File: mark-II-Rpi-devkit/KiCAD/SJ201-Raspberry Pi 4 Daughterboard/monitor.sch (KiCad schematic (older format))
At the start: 6 parts, among them J7 FanConnector, Q1 MMBT3904

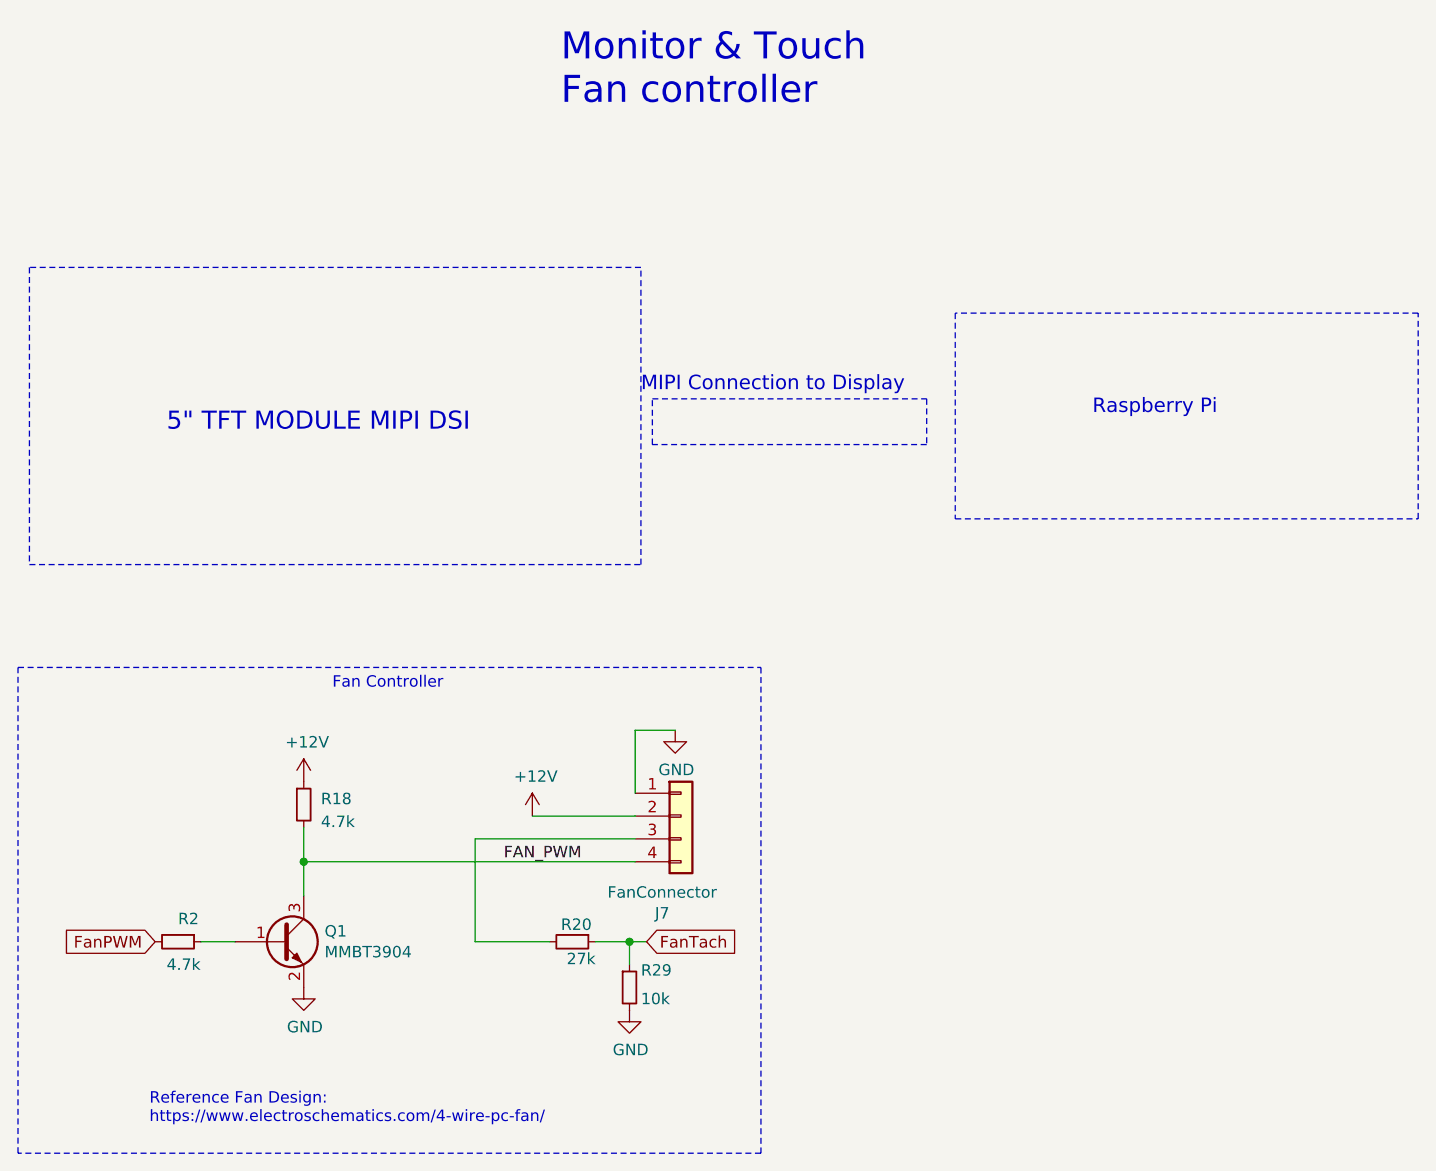
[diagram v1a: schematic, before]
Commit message: SJ-201-R6 for FAB - removed buffer IC
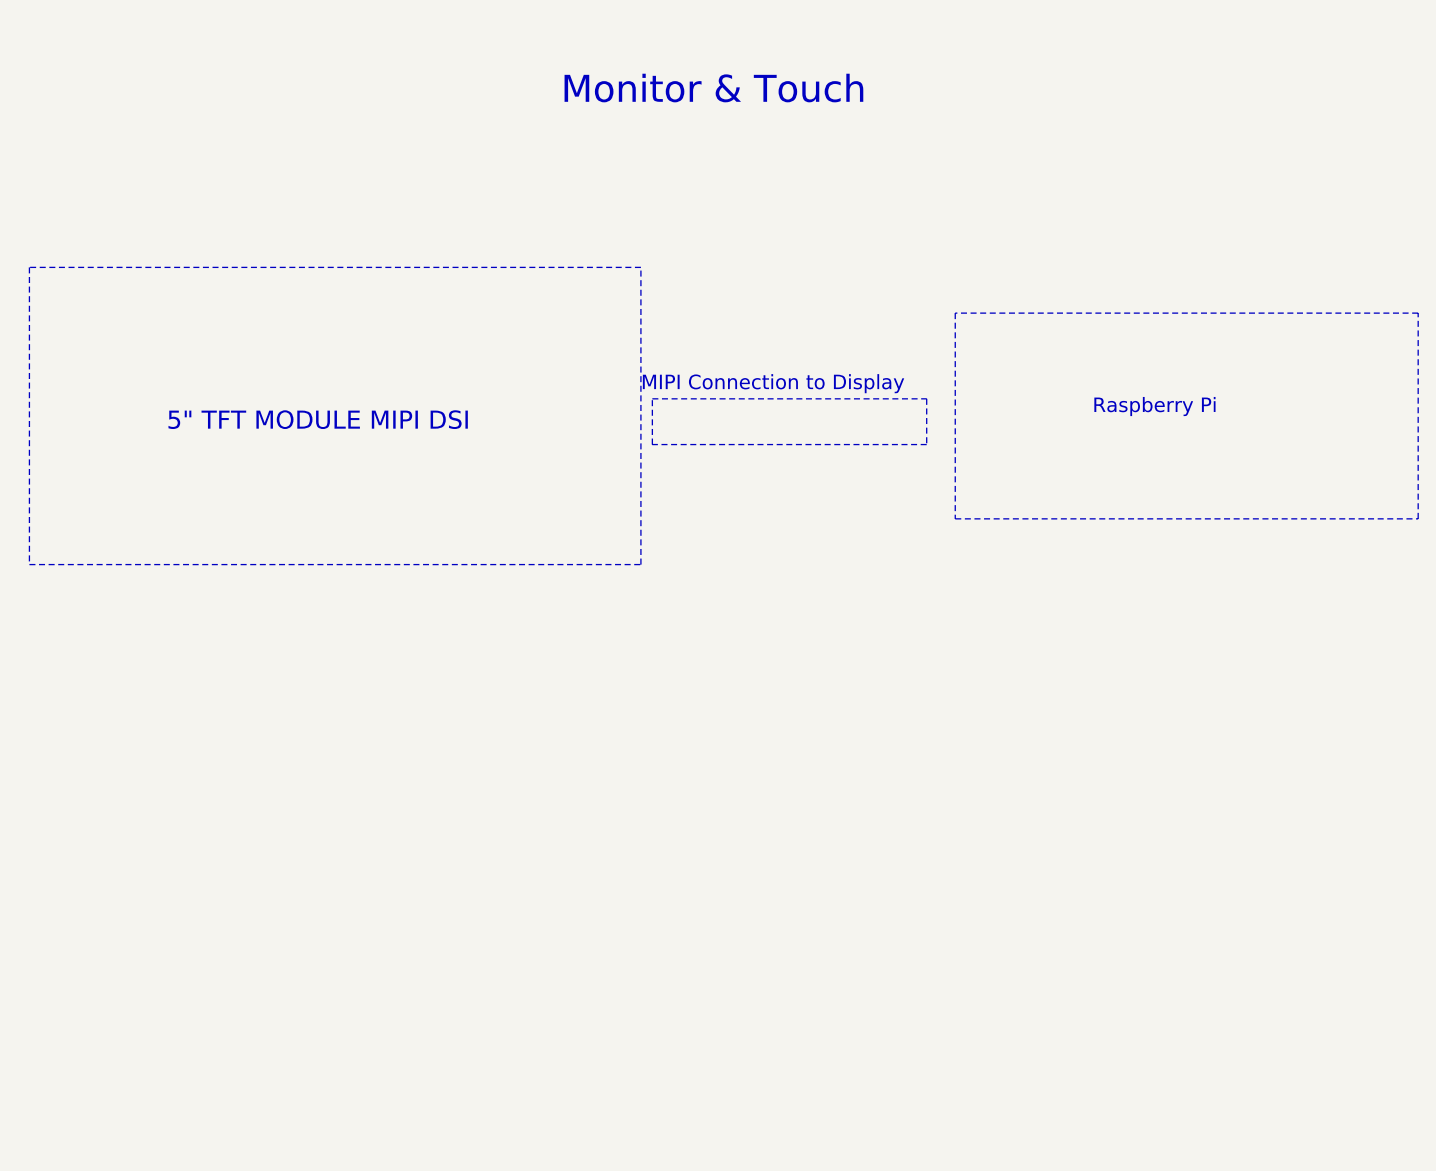
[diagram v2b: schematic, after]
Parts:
- removed J7: FanConnector, Connector:FanPinHeader_1x04_P2.54mm_Vertical, symbol Connector_Generic:Conn_01x04
- removed Q1: MMBT3904, Package_TO_SOT_SMD:SOT-23, symbol Transistor_BJT:MMBT3904
- removed R18, R2: 4.7k, Resistor_SMD:R_0402_1005Metric, symbol Device:R_Small
- removed R20: 27k, Resistor_SMD:R_0402_1005Metric, symbol Device:R_Small
- removed R29: 10k, Resistor_SMD:R_0402_1005Metric, symbol Device:R_Small
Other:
- note added: "Monitor & Touch"
- note removed: "Fan Controller"
- note removed: "Monitor & Touch\nFan controller"
- note removed: "Reference Fan Design:\nhttps://www.electroschematics.com/4-wire-pc-fan/"
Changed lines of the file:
@@
 $Descr A 11000 8500
 encoding utf-8
-Sheet 4 7
-Title ""
-Date "2020-11-22"
-Rev "Rev4 - 0.03"
-Comp "Mycroft"
-Comment1 "SJ-201-R4"
+Sheet 4 8
+Title "Monitor & Touchscreen"
+Date "2020-12-30"
+Rev "Rev5 - v1"
+Comp "Mycroft AI"
+Comment1 "SJ-201-R6"
 Comment2 ""
 Comment3 ""
@@
 $EndDescr
 Text Notes 4725 875  0    118  ~ 0
-Monitor & Touch\nFan controller
+Monitor & Touch
 Text Notes 7050 2225 0    63   ~ 0
 Raspberry Pi
@@
 Wire Notes Line
 	2400 1575 2400 2875
-$Comp
-L Transistor_BJT:MMBT3904 Q1
-U 1 1 60970DB4
-P 3500 4525
-F 0 "Q1" H 3691 4571 50  0000 L CNN
-F 1 "MMBT3904" H 3691 4480 50  0000 L CNN
-F 2 "Package_TO_SOT_SMD:SOT-23" H 3700 4450 50  0001 L CIN
-F 3 "" H 3500 4525 50  0001 L CNN
-F 4 "C20526" H 3500 4525 50  0001 C CNN "LCSC"
-	1    3500 4525
-	1    0    0    -1
-$EndComp
-$Comp
-L power:GND #PWR0117
-U 1 1 60971565
-P 3600 4725
-F 0 "#PWR0117" H 3600 4475 50  0001 C CNN
-F 1 "GND" H 3605 4552 50  0000 C CNN
-F 2 "" H 3600 4725 50  0001 C CNN
-F 3 "" H 3600 4725 50  0001 C CNN
-	1    3600 4725
-	1    0    0    -1
-$EndComp
-$Comp
-L Device:R_Small R?
-U 1 1 609730D3
-P 3050 4525
-AR Path="/5EA9C461/609730D3" Ref="R?"  Part="1"
-AR Path="/5EA9C67D/609730D3" Ref="R?"  Part="1"
-AR Path="/5EA9C76D/609730D3" Ref="R?"  Part="1"
-AR Path="/5EAB86B0/609730D3" Ref="R2"  Part="1"
-F 0 "R2" V 2950 4525 50  0000 L CNN
-F 1 "4.7k" V 3150 4475 50  0000 L CNN
-F 2 "Resistor_SMD:R_0402_1005Metric" H 3050 4525 50  0001 C CNN
-F 3 "~" H 3050 4525 50  0001 C CNN
-F 4 "0402WGF4701TCE" H 3050 4525 50  0001 C CNN "MPN"
-F 5 "C25900" H 3050 4525 50  0001 C CNN "LCSC"
-F 6 "RC0402JR-074K7L" H 3050 4525 50  0001 C CNN "Tempo"
-	1    3050 4525
-	0    1    1    0
-$EndComp
-$Comp
-L Device:R_Small R?
-U 1 1 609732C2
-P 3600 3925
-AR Path="/5EA9C461/609732C2" Ref="R?"  Part="1"
-AR Path="/5EA9C67D/609732C2" Ref="R?"  Part="1"
-AR Path="/5EA9C76D/609732C2" Ref="R?"  Part="1"
-AR Path="/5EAB86B0/609732C2" Ref="R18"  Part="1"
-F 0 "R18" H 3675 3950 50  0000 L CNN
-F 1 "4.7k" H 3675 3850 50  0000 L CNN
-F 2 "Resistor_SMD:R_0402_1005Metric" H 3600 3925 50  0001 C CNN
-F 3 "~" H 3600 3925 50  0001 C CNN
-F 4 "0402WGF4701TCE" H 3600 3925 50  0001 C CNN "MPN"
-F 5 "C25900" H 3600 3925 50  0001 C CNN "LCSC"
-F 6 "RC0402JR-074K7L" H 3600 3925 50  0001 C CNN "Tempo"
-	1    3600 3925
-	1    0    0    -1
-$EndComp
-$Comp
-L power:+12V #PWR?
-U 1 1 6098392C
-P 4600 3975
-AR Path="/5EAAC9A5/6098392C" Ref="#PWR?"  Part="1"
-AR Path="/5EA9C461/6098392C" Ref="#PWR?"  Part="1"
-AR Path="/5EAB86B0/6098392C" Ref="#PWR0158"  Part="1"
-F 0 "#PWR0158" H 4600 3825 50  0001 C CNN
-F 1 "+12V" H 4615 4148 50  0000 C CNN
-F 2 "" H 4600 3975 50  0001 C CNN
-F 3 "" H 4600 3975 50  0001 C CNN
-	1    4600 3975
-	1    0    0    -1
-$EndComp
-Text GLabel 5100 4525 2    51   Input ~ 0
-FanTach
-Wire Wire Line
-	5050 3975 4600 3975
-$Comp
-L Connector_Generic:Conn_01x04 J?
-U 1 1 60983934
-P 5250 3975
-AR Path="/5EA9C461/60983934" Ref="J?"  Part="1"
-AR Path="/5EAB86B0/60983934" Ref="J7"  Part="1"
-F 0 "J7" H 5168 3550 50  0000 C CNN
-F 1 "FanConnector" H 5168 3641 50  0000 C CNN
-F 2 "Connector:FanPinHeader_1x04_P2.54mm_Vertical" H 5250 3975 50  0001 C CNN
-F 3 "~" H 5250 3975 50  0001 C CNN
-	1    5250 3975
-	1    0    0    -1
-$EndComp
-Text GLabel 2950 4525 0    51   Input ~ 0
-FanPWM
-$Comp
-L power:GND #PWR0159
-U 1 1 60984A3E
-P 5225 3600
-F 0 "#PWR0159" H 5225 3350 50  0001 C CNN
-F 1 "GND" H 5230 3427 50  0000 C CNN
-F 2 "" H 5225 3600 50  0001 C CNN
-F 3 "" H 5225 3600 50  0001 C CNN
-	1    5225 3600
-	1    0    0    -1
-$EndComp
-Wire Wire Line
-	5225 3600 5050 3600
-Wire Wire Line
-	5050 3600 5050 3875
-Wire Wire Line
-	5050 4175 3600 4175
-Wire Wire Line
-	3600 4175 3600 4325
-Text Label 4475 4175 0    50   ~ 0
-FAN_PWM
-$Comp
-L power:+12V #PWR?
-U 1 1 60985749
-P 3600 3825
-AR Path="/5EAAC9A5/60985749" Ref="#PWR?"  Part="1"
-AR Path="/5EA9C461/60985749" Ref="#PWR?"  Part="1"
-AR Path="/5EAB86B0/60985749" Ref="#PWR0188"  Part="1"
-F 0 "#PWR0188" H 3600 3675 50  0001 C CNN
-F 1 "+12V" H 3615 3998 50  0000 C CNN
-F 2 "" H 3600 3825 50  0001 C CNN
-F 3 "" H 3600 3825 50  0001 C CNN
-	1    3600 3825
-	1    0    0    -1
-$EndComp
-Wire Wire Line
-	3600 4025 3600 4175
-Connection ~ 3600 4175
-Wire Wire Line
-	3300 4525 3150 4525
-Wire Wire Line
-	5050 4075 4350 4075
-Wire Wire Line
-	4350 4075 4350 4525
-Wire Wire Line
-	4350 4525 4675 4525
-$Comp
-L Device:R_Small R?
-U 1 1 6098617E
-P 4775 4525
-AR Path="/5EA9C461/6098617E" Ref="R?"  Part="1"
-AR Path="/5EA9C67D/6098617E" Ref="R?"  Part="1"
-AR Path="/5EA9C76D/6098617E" Ref="R?"  Part="1"
-AR Path="/5EAB86B0/6098617E" Ref="R20"  Part="1"
-F 0 "R20" V 4700 4475 50  0000 L CNN
-F 1 "27k" V 4850 4500 50  0000 L CNN
-F 2 "Resistor_SMD:R_0402_1005Metric" H 4775 4525 50  0001 C CNN
-F 3 "~" H 4775 4525 50  0001 C CNN
-F 4 "C25771" H 4775 4525 50  0001 C CNN "LCSC"
-	1    4775 4525
-	0    1    1    0
-$EndComp
-$Comp
-L power:GND #PWR0189
-U 1 1 60986B27
-P 5025 4825
-F 0 "#PWR0189" H 5025 4575 50  0001 C CNN
-F 1 "GND" H 5030 4652 50  0000 C CNN
-F 2 "" H 5025 4825 50  0001 C CNN
-F 3 "" H 5025 4825 50  0001 C CNN
-	1    5025 4825
-	1    0    0    -1
-$EndComp
-$Comp
-L Device:R_Small R?
-U 1 1 60987E5F
-P 5025 4725
-AR Path="/5EA9C461/60987E5F" Ref="R?"  Part="1"
-AR Path="/5EA9C67D/60987E5F" Ref="R?"  Part="1"
-AR Path="/5EAAC9A5/60987E5F" Ref="R?"  Part="1"
-AR Path="/5EAB86B0/60987E5F" Ref="R29"  Part="1"
-F 0 "R29" H 5075 4800 50  0000 L CNN
-F 1 "10k" H 5075 4675 50  0000 L CNN
-F 2 "Resistor_SMD:R_0402_1005Metric" H 5025 4725 50  0001 C CNN
-F 3 "~" H 5025 4725 50  0001 C CNN
-F 4 "RC0402FR-0710KL" H 5025 4725 50  0001 C CNN "MPN"
-F 5 "C25744" H 5025 4725 50  0001 C CNN "LCSC"
-	1    5025 4725
-	1    0    0    -1
-$EndComp
-Wire Wire Line
-	5100 4525 5025 4525
-Text Notes 2925 5325 0    50   ~ 0
-Reference Fan Design:\nhttps://www.electroschematics.com/4-wire-pc-fan/
-Wire Wire Line
-	5025 4625 5025 4525
-Connection ~ 5025 4525
-Wire Wire Line
-	5025 4525 4875 4525
-Text Notes 3725 3425 0    50   ~ 0
-Fan Controller
-Wire Notes Line
-	5600 3325 5600 5450
-Wire Notes Line
-	5600 5450 2350 5450
-Wire Notes Line
-	2350 5450 2350 3325
-Wire Notes Line
-	2350 3325 5600 3325
 $EndSCHEMATC
